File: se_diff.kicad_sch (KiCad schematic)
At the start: 12 parts

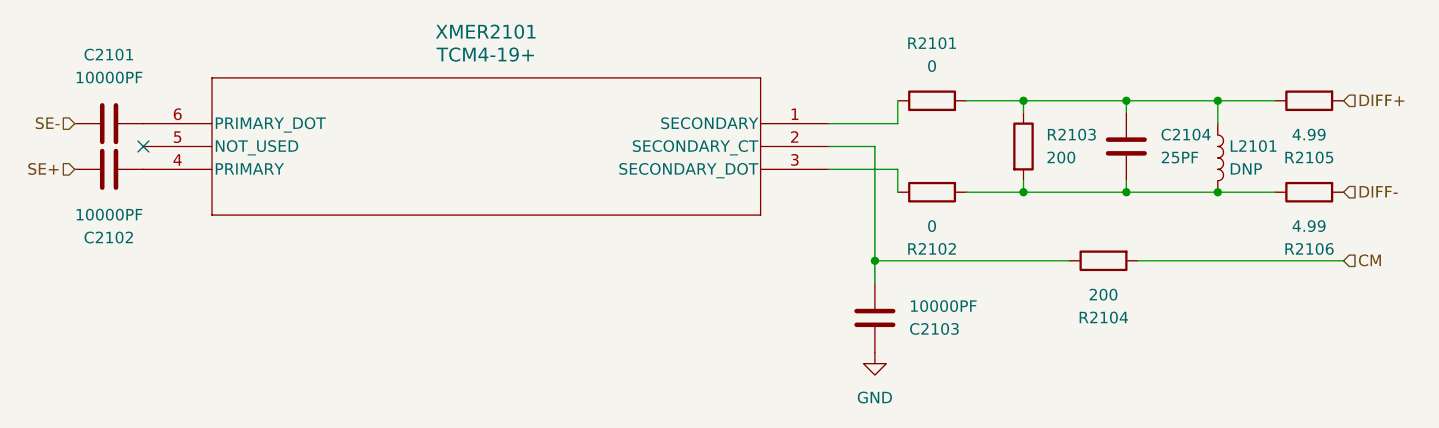
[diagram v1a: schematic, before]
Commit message: Increase layout size to accommodate more SMA connector
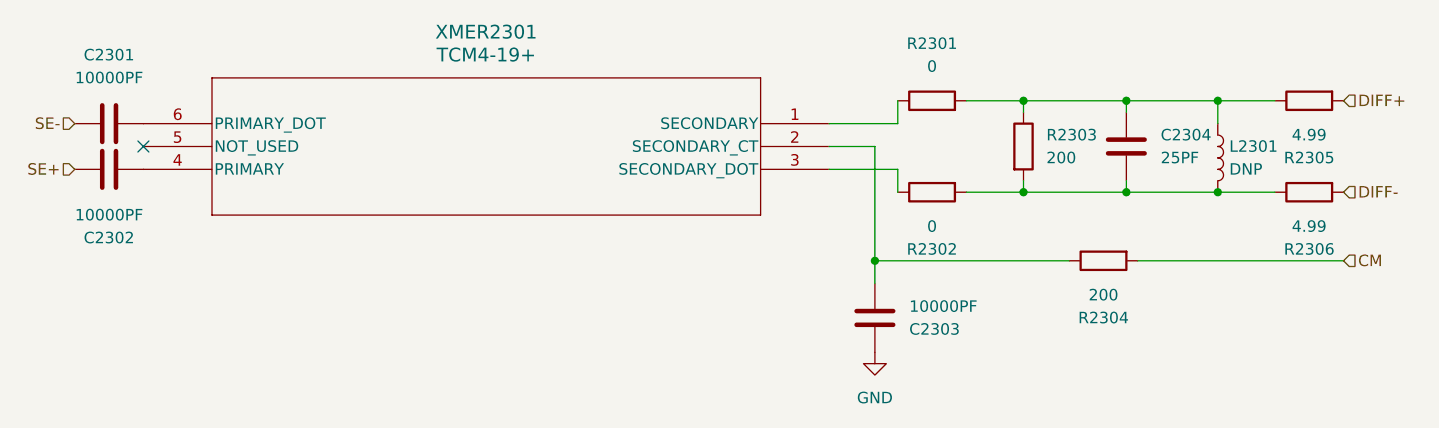
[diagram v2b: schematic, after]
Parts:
- renumbered C2101 to C2301, C2102 to C2302, C2103 to C2303, C2104 to C2304, L2101 to L2301, R2101 to R2301, R2102 to R2302, R2103 to R2303, R2104 to R2304, R2105 to R2305, R2106 to R2306, XMER2101 to XMER2301
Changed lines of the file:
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@@
 		(on_board yes)
 		(dnp no)
-		(property "Reference" "R2106"
+		(property "Reference" "R2306"
 			(at 227.33 90.17 90)
 			(effects
@@
 		(dnp no)
 		(fields_autoplaced yes)
-		(property "Reference" "L2101"
+		(property "Reference" "L2301"
 			(at 218.44 78.7399 0)
 			(effects
@@
 		(dnp no)
 		(fields_autoplaced yes)
-		(property "Reference" "XMER2101"
+		(property "Reference" "XMER2301"
 			(at 135.89 66.04 0)
 			(effects
@@
 		(on_board yes)
 		(dnp no)
-		(property "Reference" "C2102"
+		(property "Reference" "C2302"
 			(at 93.98 88.9 90)
 			(effects
@@
 		(on_board yes)
 		(dnp no)
-		(property "Reference" "C2101"
+		(property "Reference" "C2301"
 			(at 93.98 68.58 90)
 			(effects
@@
 		(dnp no)
 		(fields_autoplaced yes)
-		(property "Reference" "R2103"
+		(property "Reference" "R2303"
 			(at 198.12 77.4699 0)
 			(effects
@@
 		(on_board yes)
 		(dnp no)
-		(property "Reference" "R2101"
+		(property "Reference" "R2301"
 			(at 185.42 67.31 90)
 			(effects
@@
 		(on_board yes)
 		(dnp no)
-		(property "Reference" "R2102"
+		(property "Reference" "R2302"
 			(at 185.42 90.17 90)
 			(effects
@@
 		(dnp no)
 		(fields_autoplaced yes)
-		(property "Reference" "C2104"
+		(property "Reference" "C2304"
 			(at 210.82 77.4699 0)
 			(effects
@@
 		(on_board yes)
 		(dnp no)
-		(property "Reference" "C2103"
+		(property "Reference" "C2303"
 			(at 182.88 99.0601 0)
 			(effects
@@
 		(dnp no)
 		(fields_autoplaced yes)
-		(property "Reference" "#PWR02101"
+		(property "Reference" "#PWR02301"
 			(at 179.07 107.95 0)
 			(effects
@@
 		(on_board yes)
 		(dnp no)
-		(property "Reference" "R2105"
+		(property "Reference" "R2305"
 			(at 227.33 80.01 90)
 			(effects
@@
 		(on_board yes)
 		(dnp no)
-		(property "Reference" "R2104"
+		(property "Reference" "R2304"
 			(at 204.47 97.79 90)
 			(effects
